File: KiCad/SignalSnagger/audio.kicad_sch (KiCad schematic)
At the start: 16 parts, among them J301 AudioJack4, U301 LM386

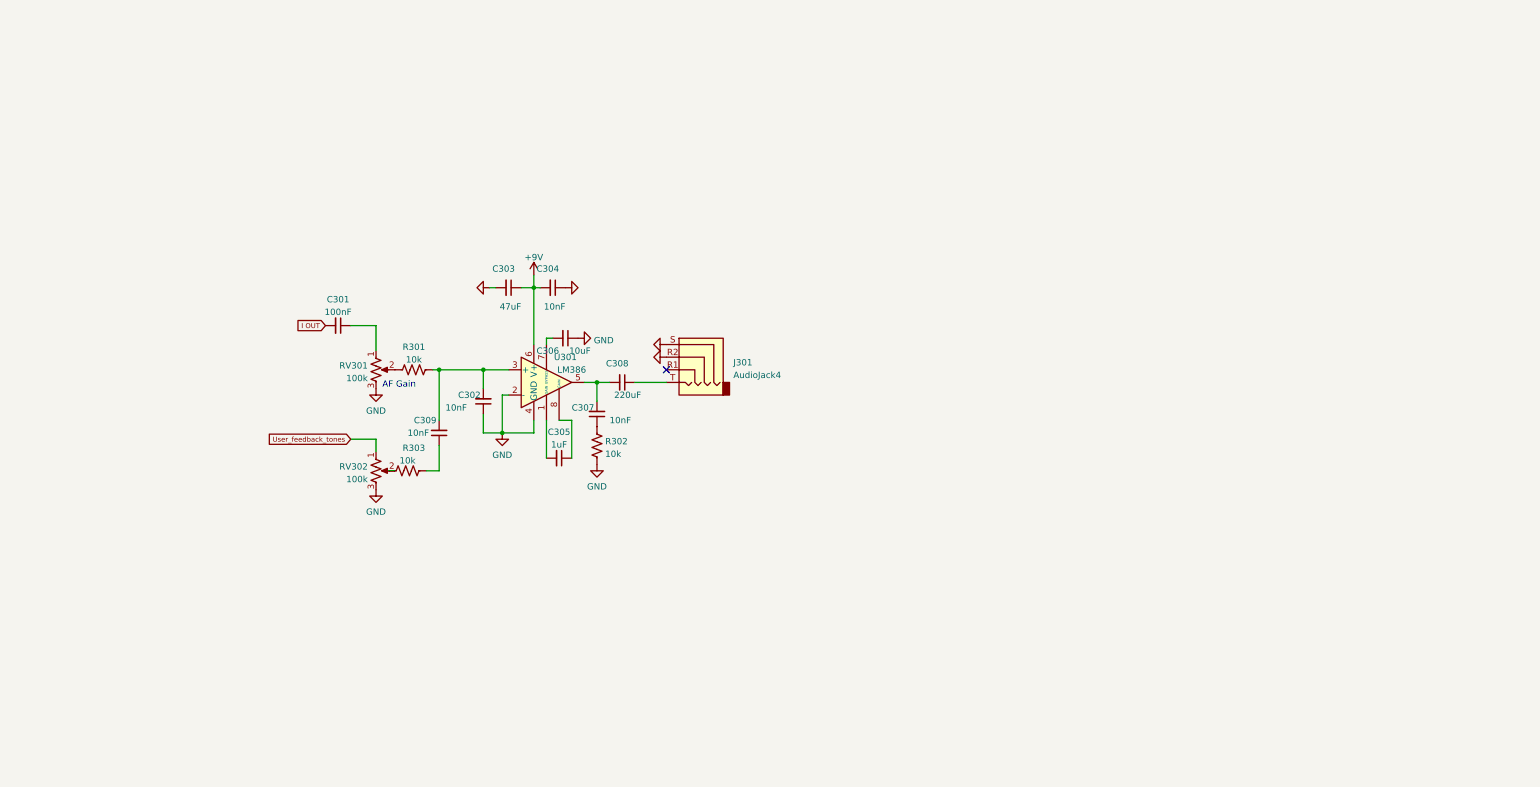
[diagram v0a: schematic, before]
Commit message: Ver 0.15
Schematic changes
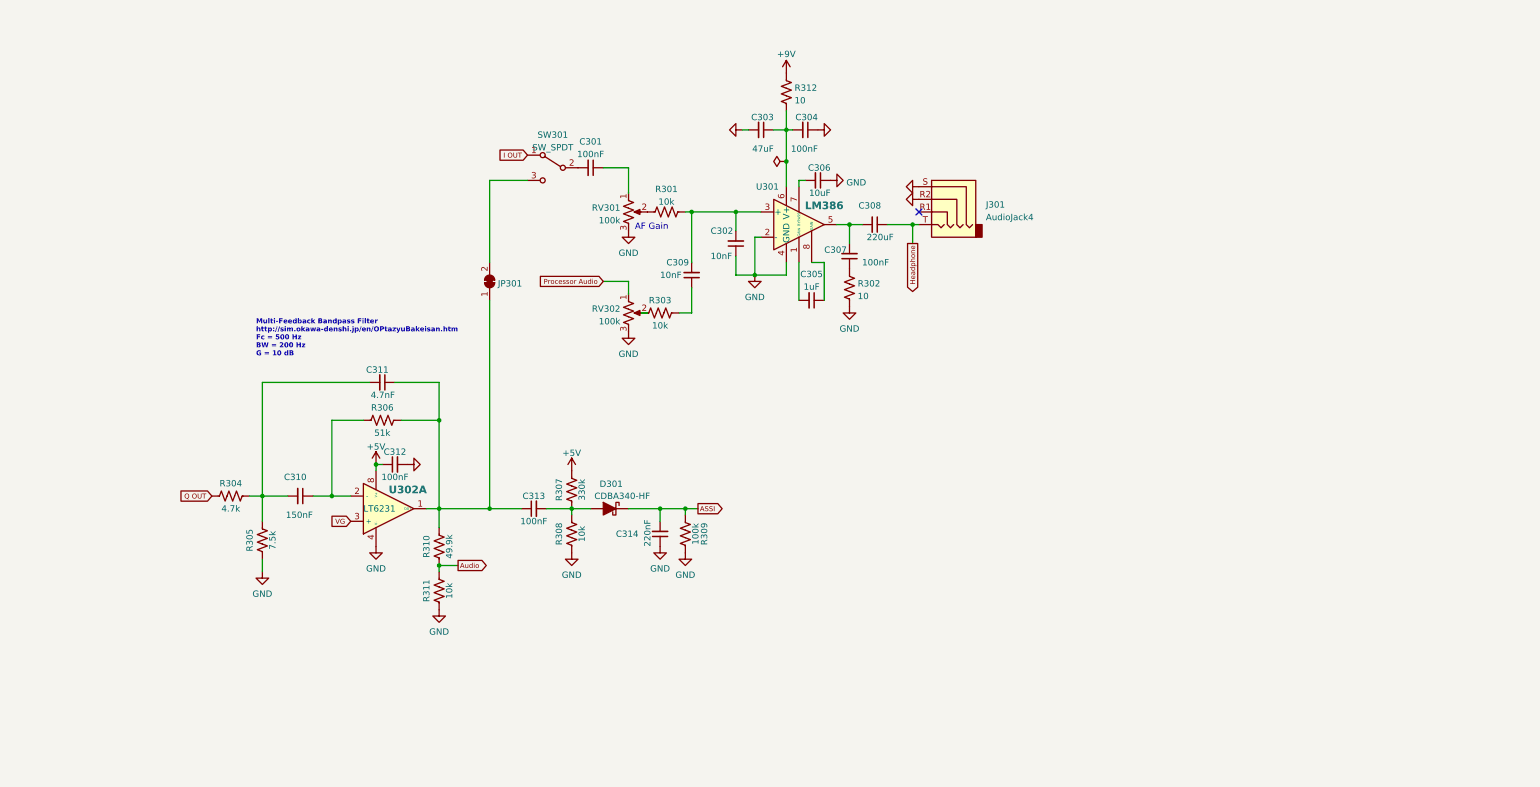
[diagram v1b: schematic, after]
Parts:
- added C310: 150nF, symbol Device:C_Small
- added C311: 4.7nF, symbol Device:C_Small
- added C312, C313: 100nF, symbol Device:C_Small
- added C314: 220nF, symbol Device:C_Small
- added D301: CDBA340-HF, Diode_SMD:D_SMA, symbol Diode:CDBA340-HF
- added JP301: (no value), symbol Jumper:SolderJumper_2_Bridged
- added R304: 4.7k, symbol Device:R_US
- added R305: 7.5k, symbol Device:R_US
- added R306: 51k, symbol Device:R_US
- added R307: 330k, symbol Device:R_US
- added R308, R311: 10k, symbol Device:R_US
- added R309: 100k, symbol Device:R_US
- added R310: 49.9k, symbol Device:R_US
- added R312: 10, symbol Device:R_US
- added SW301: SW_SPDT, symbol Switch:SW_SPDT
- added U302: LT6231, Package_TO_SOT_SMD:TSOT-23-6, symbol Amplifier_Operational:LT6231
- C304, C307: value 10nF -> 100nF
- R302: value 10k -> 10
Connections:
- net +9V: now also R312.1; no longer C303.1, C304.2, U301.6 (V+)
- net GND: now also C312.2, C314.1, R305.2, R308.2, R309.2, R311.2, U302.4 (V-)
- net I OUT: now also SW301.1 (A); no longer C301.2
- net Headphone: now reaches C308.1, J301.T
- net User_feedback_tones renamed Processor Audio
- new net: C303.1, C304.2, R312.2, U301.6 (V+)
- new net: C311.1, C313.1, JP301.1 (A), R306.2, R310.1, U302.1 (OUT)
- new net: JP301.2 (B), SW301.3 (C)
- new net: C313.2, D301.2 (A), R307.2, R308.1
- new net: C310.1, R306.1, U302.2 (-)
- new net: C310.2, C311.2, R304.2, R305.1
- new net: C301.2, SW301.2 (B)
- new net +5V: C312.1, R307.1, U302.8 (V+)
- new net ASSI: C314.2, D301.1 (K), R309.1
- new net Audio: R310.2, R311.1
- new net Q OUT: R304.1
- new net VG: U302.3 (+)
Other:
- note added: "Multi-Feedback Bandpass Filter http://sim.okawa-denshi.jp/en/OPtazyuBakeisan.htm Fc = 500 Hz BW = 200 Hz G = 10 dB"
- moved on the sheet: C301, C302, C303, C304, C305, C306, C307, C308, C309, J301, R301, R302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

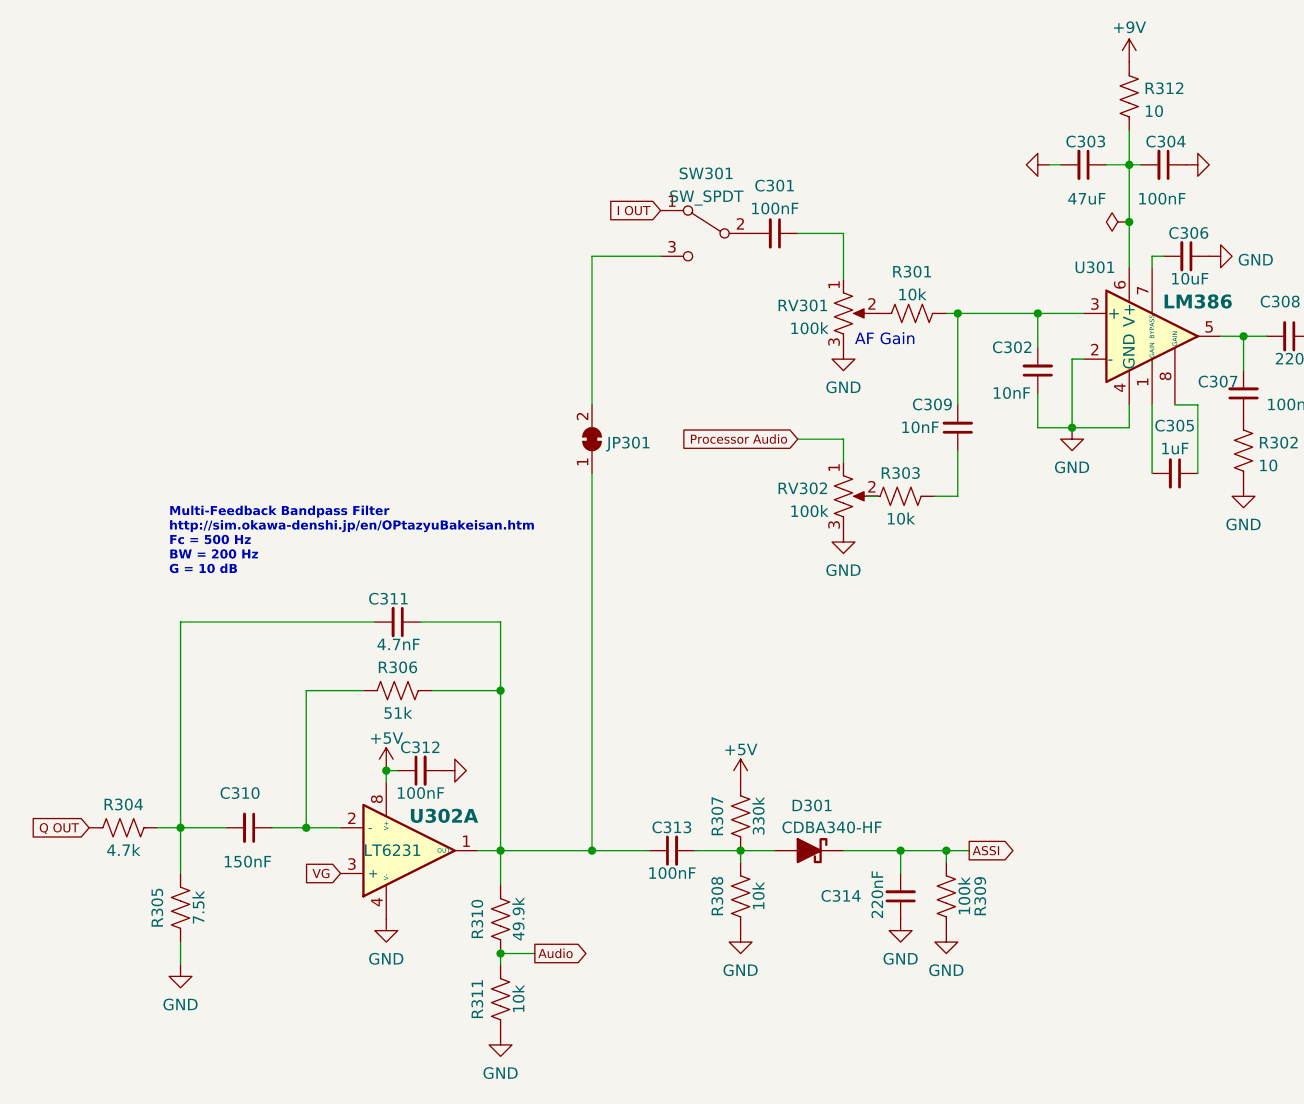
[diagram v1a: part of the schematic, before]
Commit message: Schematic Updates
Added display and rotary encoder
Added Jerry's changes based on testing
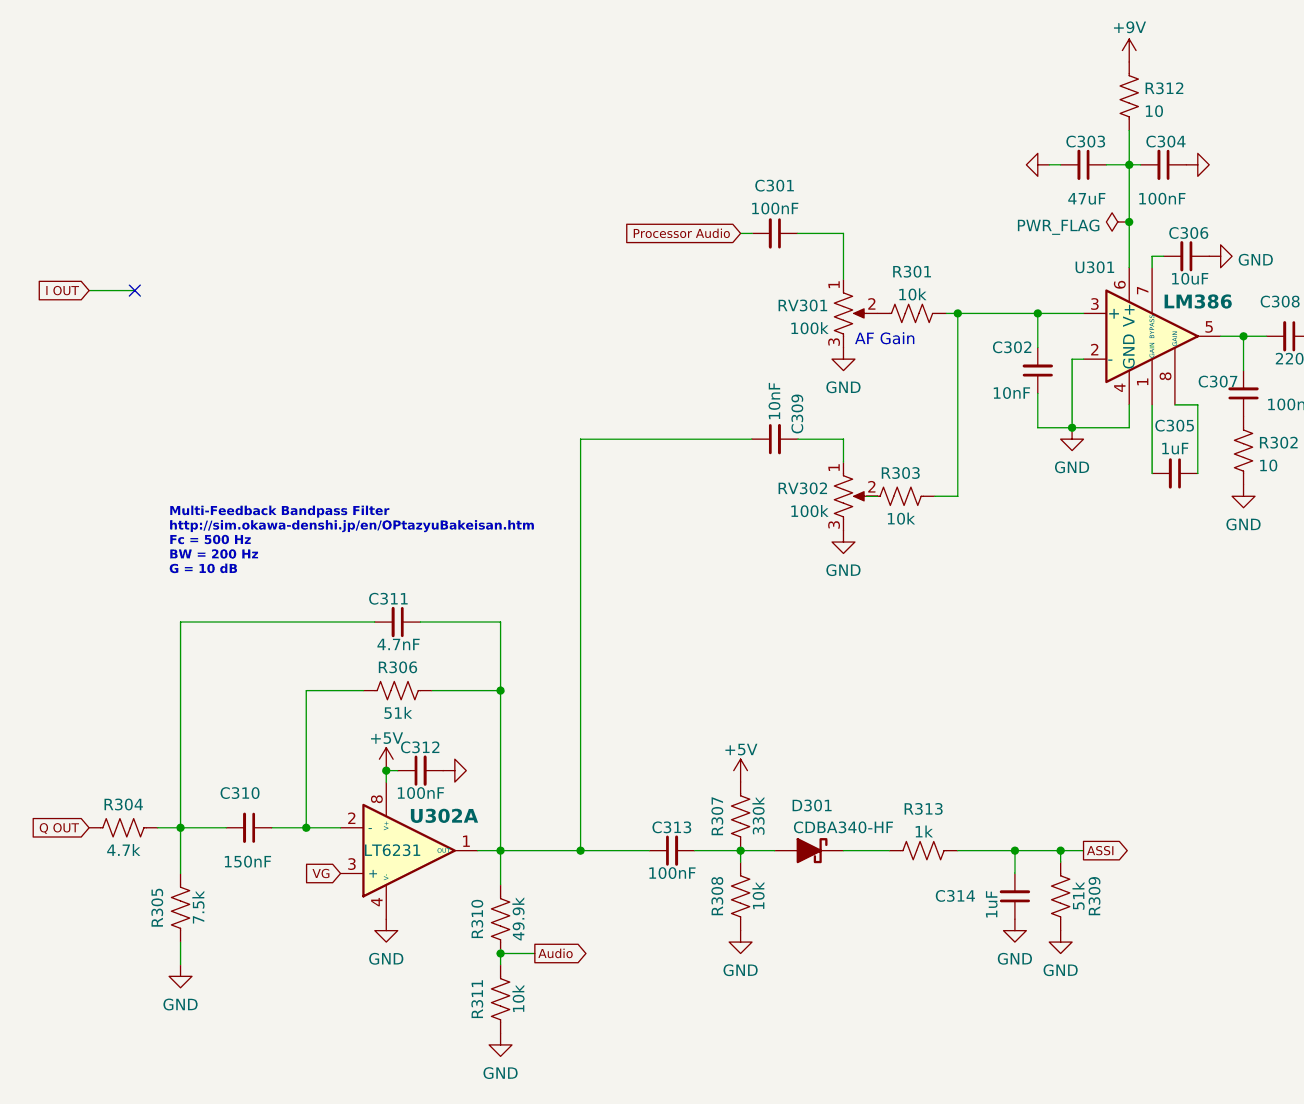
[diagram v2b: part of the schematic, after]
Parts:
- removed JP301: (no value), symbol Jumper:SolderJumper_2_Bridged
- removed SW301: SW_SPDT, symbol Switch:SW_SPDT
- added R313: 1k, symbol Device:R_US
- C314: value 220nF -> 1uF
- R309: value 100k -> 51k
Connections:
- net ASSI: now also R313.2; no longer D301.1 (K)
- net Processor Audio: now also C301.2; no longer RV302.1
- net at C311.1, C313.1, R306.2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: now also C309.1
- net at C302.2, R301.2, U301.3 (+): now also R303.2; no longer C309.2
- new net: D301.1 (K), R313.1
- new net: C309.2, RV302.1
- no-connect marks 1 -> 2
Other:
- moved on the sheet: C309, C314, R309
